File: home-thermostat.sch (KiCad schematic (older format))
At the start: 50 parts

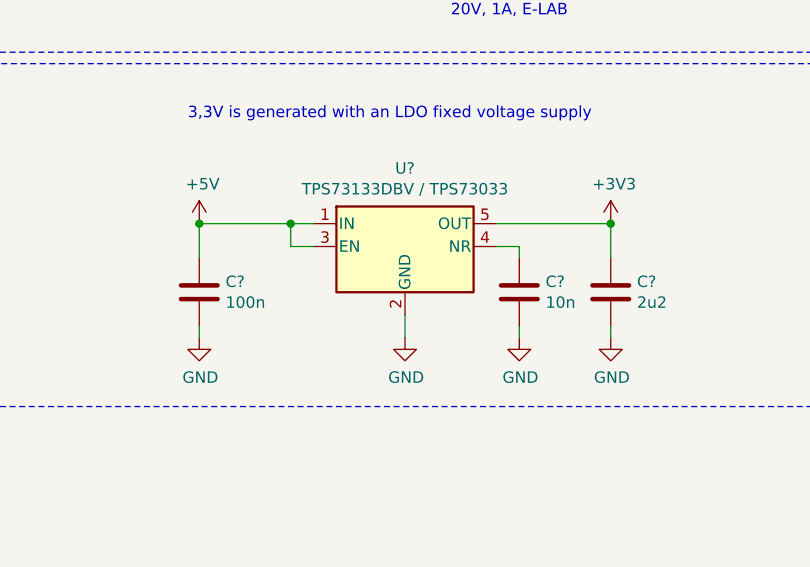
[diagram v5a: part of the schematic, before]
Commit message: Exchanged 3,3V LDO with one I found at home.
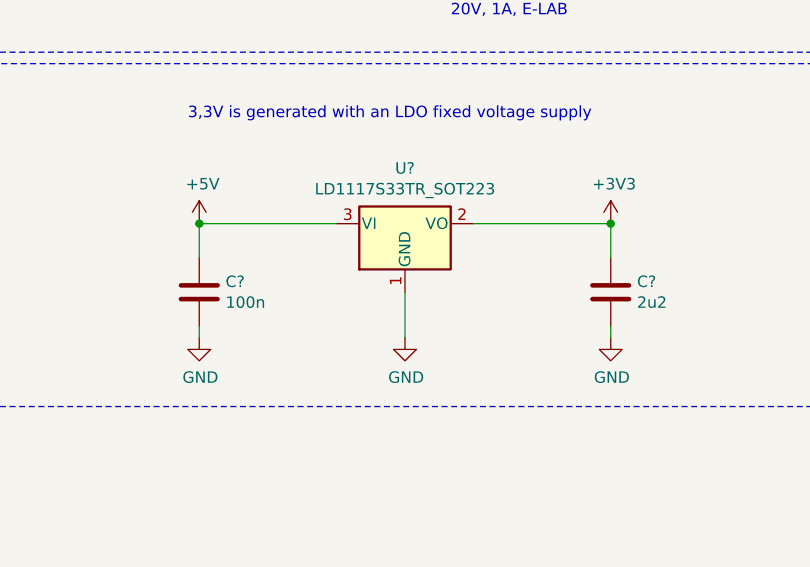
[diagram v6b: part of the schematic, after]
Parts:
- removed C?: 10n, symbol Device:C
- removed U?: TPS73133DBV / TPS73033, Package_TO_SOT_SMD:SOT-23-5, symbol Regulator_Linear:TPS73133DBV
- added U?: LD1117S33TR_SOT223, Package_TO_SOT_SMD:SOT-223-3_TabPin2, symbol Regulator_Linear:LD1117S33TR_SOT223
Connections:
- net +3V3: now also U?.2 (VO)
- net +5V: now also U?.3 (VI)
- net GND: now also U?.1 (GND)
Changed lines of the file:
@@
 Connection ~ 7700 3500
-$Comp
-L Regulator_Linear:TPS73133DBV U?
-U 1 1 5EABE9E0
-P 9050 5250
-AR Path="/5E8AC4D3/5EABE9E0" Ref="U?"  Part="1"
-AR Path="/5EABE9E0" Ref="U?"  Part="1"
-F 0 "U?" H 9050 5592 50  0000 C CNN
-F 1 "TPS73133DBV / TPS73033" H 9050 5501 50  0000 C CNN
-F 2 "Package_TO_SOT_SMD:SOT-23-5" H 9050 5575 50  0001 C CIN
-F 3 "http://www.ti.com/lit/ds/symlink/tps731.pdf" H 9050 5200 50  0001 C CNN
-	1    9050 5250
-	1    0    0    -1
-$EndComp
 $Comp
 L Device:C C?
@@
 Wire Wire Line
 	8150 5300 8150 5150
-Wire Wire Line
-	8150 5150 8550 5150
-Wire Wire Line
-	8650 5250 8550 5250
-Wire Wire Line
-	8550 5250 8550 5150
-Connection ~ 8550 5150
-Wire Wire Line
-	8550 5150 8650 5150
-$Comp
-L Device:C C?
-U 1 1 5EABE9F2
-P 9550 5450
-AR Path="/5E8AC4D3/5EABE9F2" Ref="C?"  Part="1"
-AR Path="/5EABE9F2" Ref="C?"  Part="1"
-F 0 "C?" H 9665 5496 50  0000 L CNN
-F 1 "10n" H 9665 5405 50  0000 L CNN
-F 2 "" H 9588 5300 50  0001 C CNN
-F 3 "~" H 9550 5450 50  0001 C CNN
-	1    9550 5450
-	1    0    0    -1
-$EndComp
 $Comp
 L Device:C C?
@@
 Wire Wire Line
 	9950 5300 9950 5150
-Wire Wire Line
-	9950 5150 9450 5150
-Wire Wire Line
-	9450 5250 9550 5250
-Wire Wire Line
-	9550 5250 9550 5300
 $Comp
 L power:+5V #PWR?
@@
 $Comp
 L power:GND #PWR?
-U 1 1 5EABEA17
-P 9550 5650
-AR Path="/5E8AC4D3/5EABEA17" Ref="#PWR?"  Part="1"
-AR Path="/5EABEA17" Ref="#PWR?"  Part="1"
-F 0 "#PWR?" H 9550 5400 50  0001 C CNN
-F 1 "GND" H 9555 5477 50  0000 C CNN
-F 2 "" H 9550 5650 50  0001 C CNN
-F 3 "" H 9550 5650 50  0001 C CNN
-	1    9550 5650
-	1    0    0    -1
-$EndComp
-Wire Wire Line
-	9550 5650 9550 5600
-$Comp
-L power:GND #PWR?
 U 1 1 5EABEA1E
 P 9050 5650
@@
 	1    0    0    -1
 $EndComp
-Wire Wire Line
-	9050 5650 9050 5550
 $Comp
 L power:GND #PWR?
@@
 Wire Wire Line
 	10500 1100 10500 1200
+$Comp
+L Regulator_Linear:LD1117S33TR_SOT223 U?
+U 1 1 5F0DC12F
+P 9050 5150
+F 0 "U?" H 9050 5392 50  0000 C CNN
+F 1 "LD1117S33TR_SOT223" H 9050 5301 50  0000 C CNN
+F 2 "Package_TO_SOT_SMD:SOT-223-3_TabPin2" H 9050 5350 50  0001 C CNN
+F 3 "http://www.st.com/st-web-ui/static/active/en/resource/technical/document/datasheet/CD00000544.pdf" H 9150 4900 50  0001 C CNN
+	1    9050 5150
+	1    0    0    -1
+$EndComp
+Wire Wire Line
+	9050 5450 9050 5650
+Wire Wire Line
+	8150 5150 8750 5150
+Wire Wire Line
+	9350 5150 9950 5150
 $EndSCHEMATC

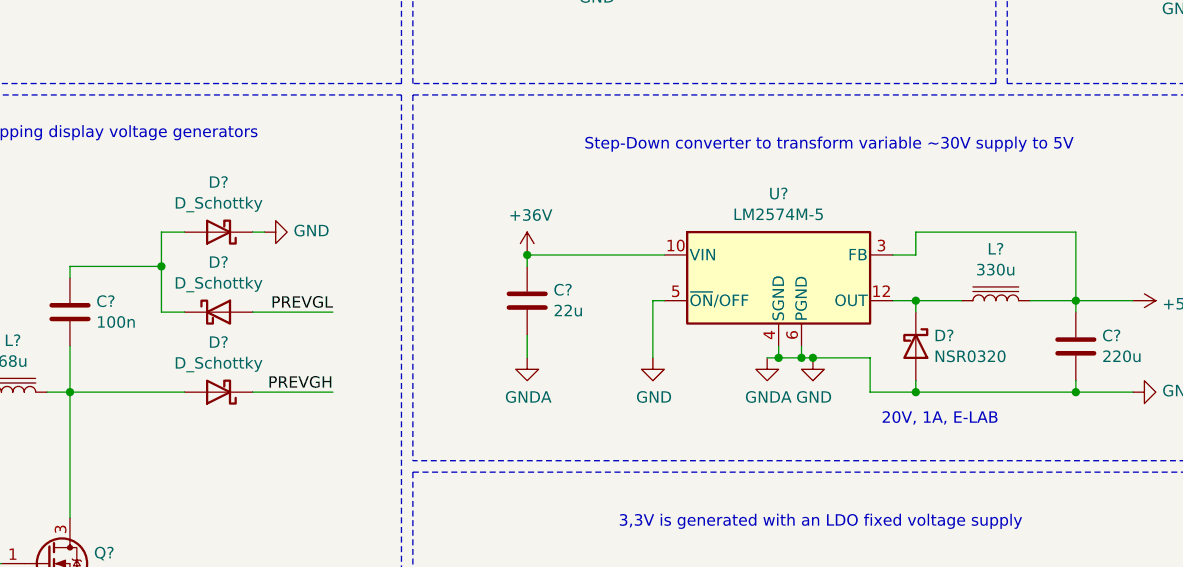
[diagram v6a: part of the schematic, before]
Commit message: Exchanged AVR crystal with one I already have.
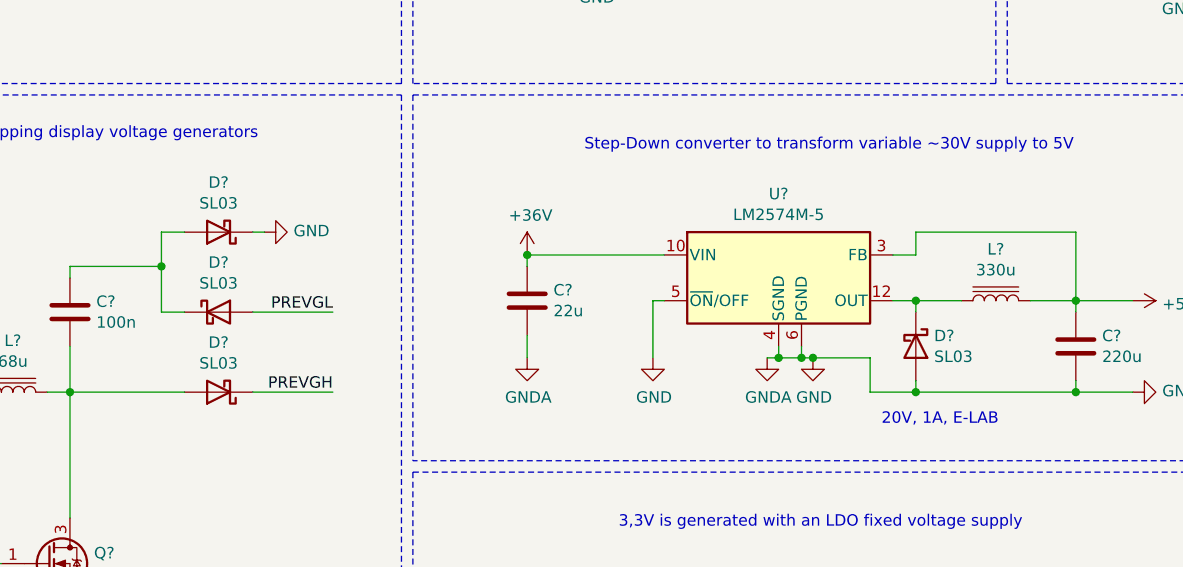
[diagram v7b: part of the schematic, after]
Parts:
- D?: value NSR0320 -> SL03
- D? (x3): value D_Schottky -> SL03
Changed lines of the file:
@@
 AR Path="/5EABE97B" Ref="D?"  Part="1"
 F 0 "D?" V 9354 3980 50  0000 L CNN
-F 1 "NSR0320" V 9445 3980 50  0000 L CNN
+F 1 "SL03" V 9445 3980 50  0000 L CNN
 F 2 "" H 9400 3900 50  0001 C CNN
 F 3 "~" H 9400 3900 50  0001 C CNN
@@
 AR Path="/5EB12646" Ref="D?"  Part="1"
 F 0 "D?" H 6350 3967 50  0000 C CNN
-F 1 "D_Schottky" H 6350 3876 50  0000 C CNN
+F 1 "SL03" H 6350 3876 50  0000 C CNN
 F 2 "" H 6350 3750 50  0001 C CNN
 F 3 "~" H 6350 3750 50  0001 C CNN
@@
 AR Path="/5EB1264C" Ref="D?"  Part="1"
 F 0 "D?" H 6350 3183 50  0000 C CNN
-F 1 "D_Schottky" H 6350 3274 50  0000 C CNN
+F 1 "SL03" H 6350 3274 50  0000 C CNN
 F 2 "" H 6350 3400 50  0001 C CNN
 F 3 "~" H 6350 3400 50  0001 C CNN
@@
 AR Path="/5EB12662" Ref="D?"  Part="1"
 F 0 "D?" H 6350 3883 50  0000 C CNN
-F 1 "D_Schottky" H 6350 3974 50  0000 C CNN
+F 1 "SL03" H 6350 3974 50  0000 C CNN
 F 2 "" H 6350 4100 50  0001 C CNN
 F 3 "~" H 6350 4100 50  0001 C CNN

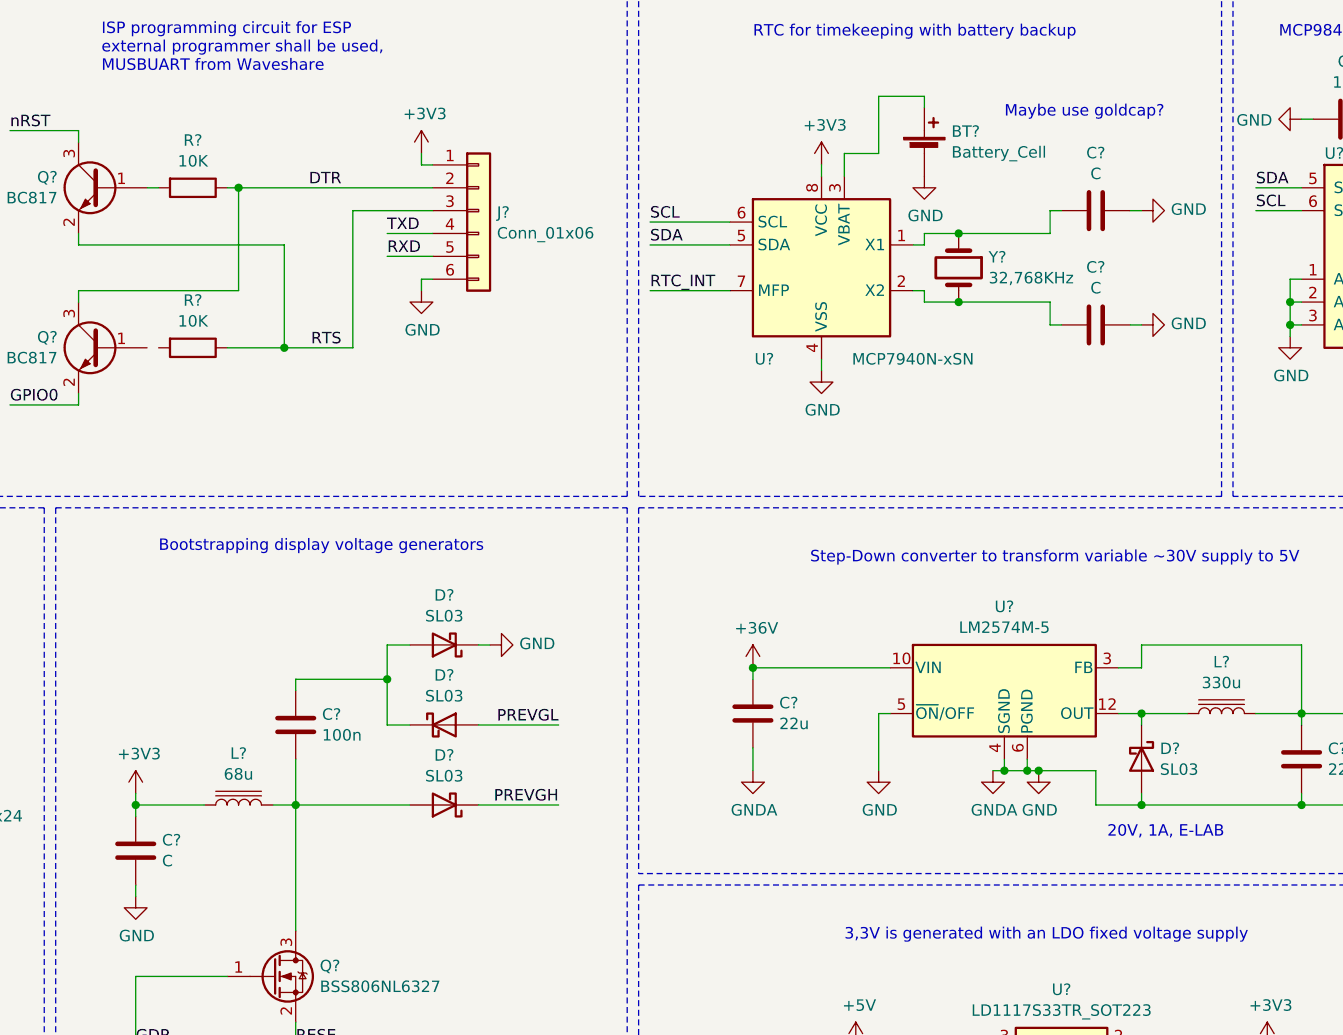
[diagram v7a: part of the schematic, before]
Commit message: Started adding footprints.
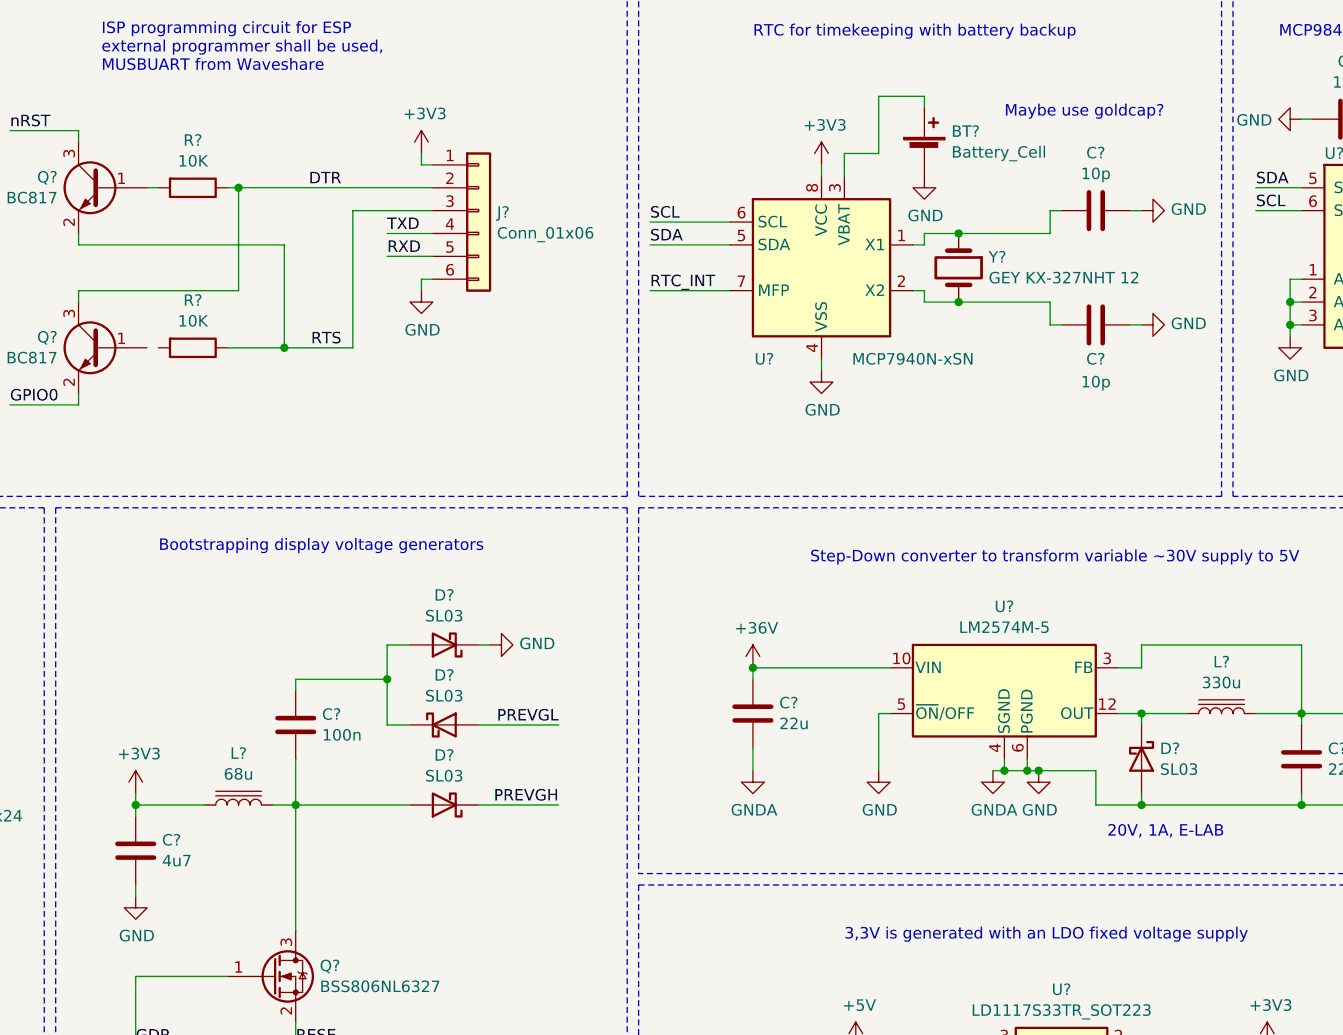
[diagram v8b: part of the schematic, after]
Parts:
- BT?: footprint (none) -> Battery:BatteryHolder_Keystone_3002_1x2032
- C? (x14): footprint (none) -> Capacitor_SMD:C_0603_1608Metric
- C? (x2): value C -> 10p; footprint (none) -> Capacitor_SMD:C_0603_1608Metric
- C?: value C -> 4u7; footprint (none) -> Capacitor_SMD:C_0603_1608Metric
- J?: footprint (none) -> Connector_FFC-FPC:TE_2-1734839-4_1x24-1MP_P0.5mm_Horizontal
- Y?: value 32,768KHz -> GEY KX-327NHT 12; footprint (none) -> Crystal:Crystal_SMD_3215-2Pin_3.2x1.5mm
